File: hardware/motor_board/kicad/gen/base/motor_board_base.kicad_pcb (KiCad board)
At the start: 4 copper layers, 75 x 35 mm, 237 parts, among them J1 BOOMELE_1.27-2x10P, J2 WAFER-SH1.0-6PWB, J3 WAFER-SH1.0-6PWB, J4 S5B-XH-A, Q1 HYG015N04LS1C2, Q2 HYG015N04LS1C2, Q3 HYG015N04LS1C2, Q4 HYG015N04LS1C2, Q5 HYG015N04LS1C2, Q6 HYG015N04LS1C2, Q7 HYG015N04LS1C2, Q8 HYG015N04LS1C2, U1 STM32G474RET6, U10 SN74LVC3G17DCUR, U11 TPS22945DCKR, U12 TPS22945DCKR, U13 LM74502DDFR, U14 74LVC1G17SE-7, U2 DRV8323RHRGZR, U3 DRV8316CRRGFR, U4 DRV8316CRRGFR, U5 AP2112K-3.3TRG1, U6 SN74LVC08APWR, U7 INA239AIDGSR, U8 BQ76907RGRR, U9 SN74LVC3G17DCUR

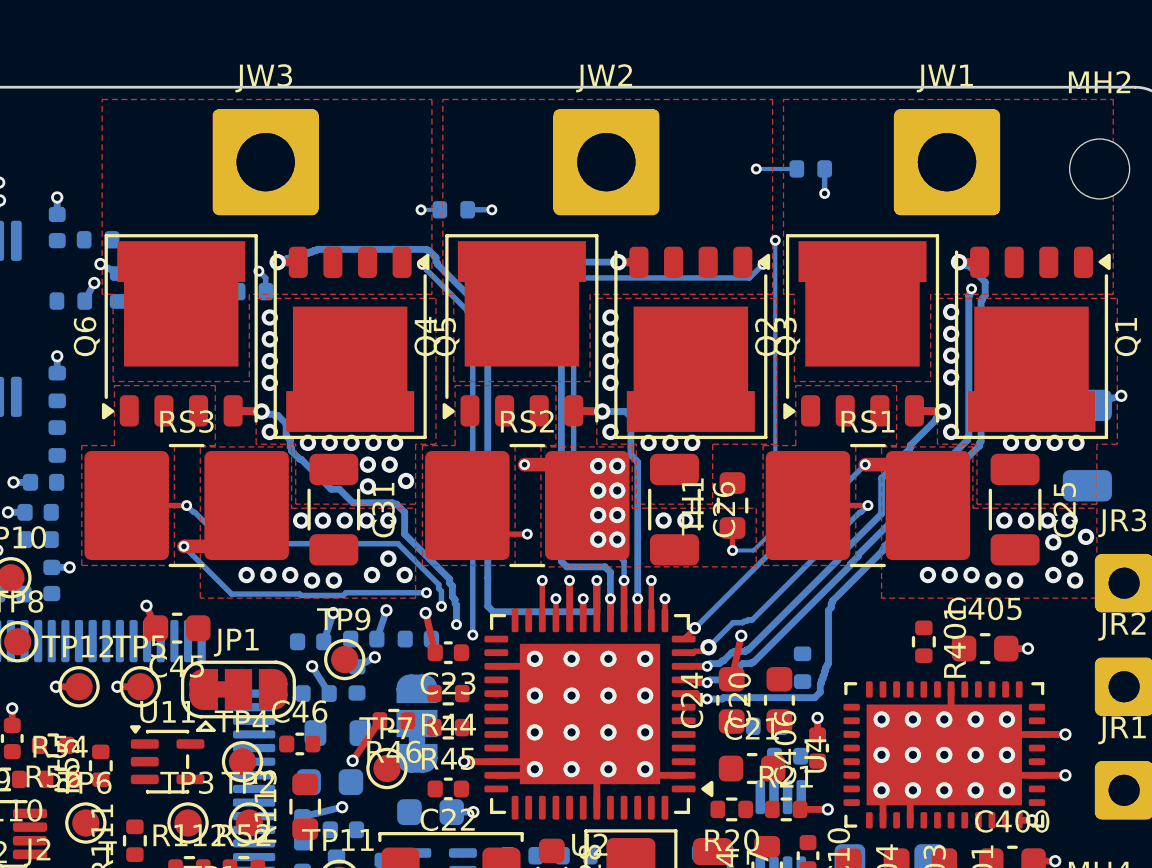
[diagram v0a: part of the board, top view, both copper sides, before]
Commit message: motor_board routing block 1: weapon gate drive + Kelvin sense (all 15 nets, DRC 0)
Scripted interactive-style routing: grid router (router.py) for open ground, hand-planned
fixed geometry (route_blocks.py) for U2's fan-out and the bundle orderings. Base-board
edits (base_edits.py): NT1-3 flat in the shunt pad gaps, R24/R62 moved, five via-field
vias dropped for channels, L3 VBAT feed trimmed to leave a front lane strip for the
divided-phase/NTC lines. Min via 0.4/0.2, Gate class 0.25 mm.

Co-Authored-By: Claude Opus 5.5 (1M context) <noreply@anthropic.com>
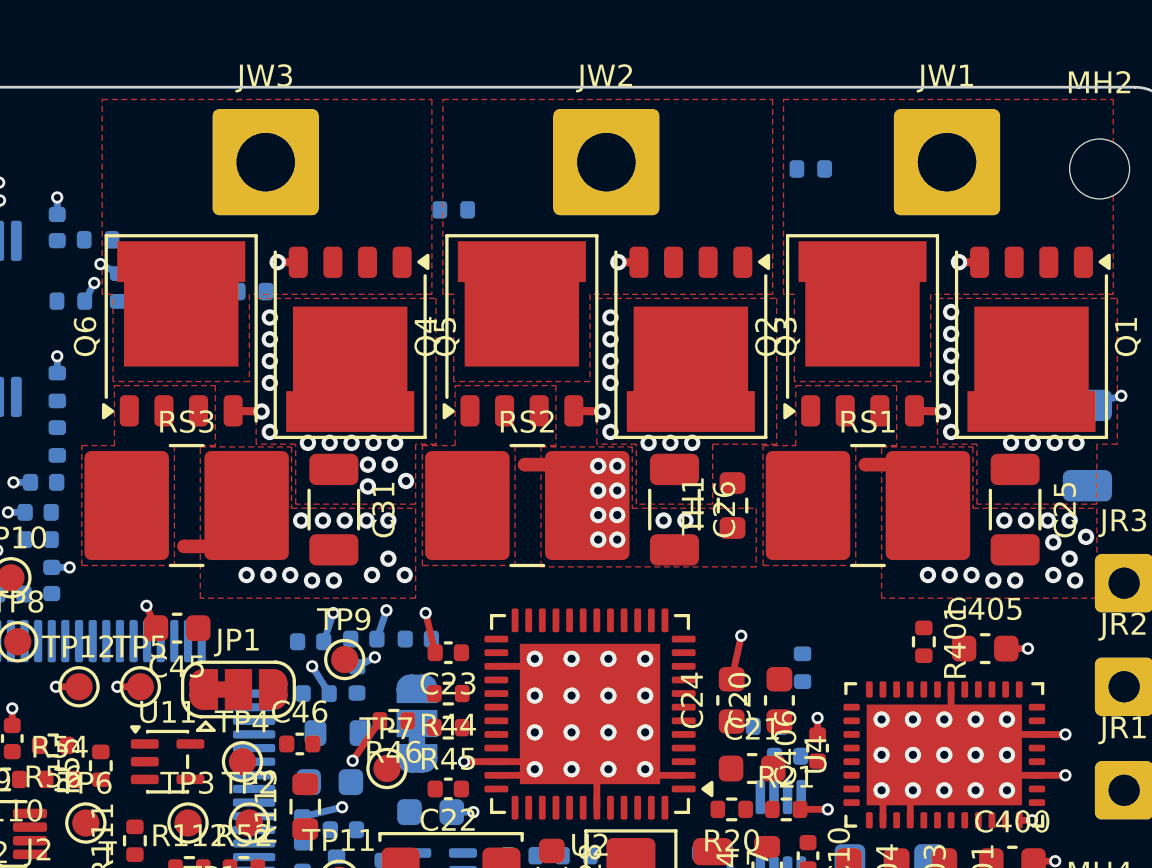
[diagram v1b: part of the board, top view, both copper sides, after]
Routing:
- net /weapon/W_GHC: track 26.9 -> 0.76 mm, vias 2 -> 1
- net /weapon/W_GHA: track 24.5 -> 0.76 mm, vias 2 -> 1
- net /weapon/W_B: track 21.8 -> 0.00 mm, vias 3 -> 0
- net /weapon/W_C: track 21.1 -> 0.00 mm, vias 4 -> 0
- net /weapon/W_A: track 20.6 -> 0.00 mm, vias 3 -> 0
- net /weapon/W_GLC: track 20.1 -> 1.05 mm, vias 3 -> 1
- net /weapon/W_SLC: track 17.3 -> 0.00 mm, vias 3 -> 0
- net /weapon/W_GHB: track 17.2 -> 0.76 mm, vias 2 -> 1
- net /weapon/W_SNC: track 15.3 -> 0.00 mm, vias 3 -> 0
- net /weapon/W_GLA: track 15.1 -> 1.05 mm, vias 2 -> 1
- net W_NTC: track 13.3 -> 0.00 mm, vias 2 -> 0
- net /weapon/W_SLA: track 9.90 -> 0.00 mm, vias 2 -> 0
- net /weapon/W_SNB: track 9.75 -> 0.00 mm, vias 2 -> 0
- net /weapon/W_SNA: track 9.31 -> 0.00 mm, vias 2 -> 0
- net /weapon/W_GLB: track 9.48 -> 1.05 mm, vias 2 -> 1
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
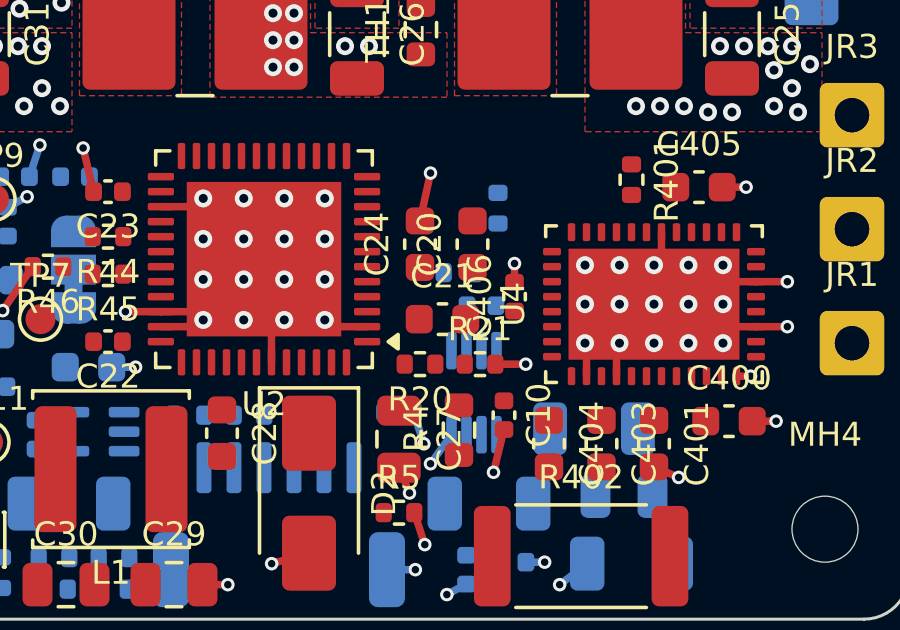
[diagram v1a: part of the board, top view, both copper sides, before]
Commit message: motor_board routing block 2: U2 local (buck loop, charge pump lanes, straps, FB/EN dividers), DRC 0
Charge-pump caps C20/C21 swapped (C20 flipped) so pins 5/4/3 fan out without crossing;
R20/R21 0.1 mm rearward for courtyard room.

Co-Authored-By: Claude Opus 5.5 (1M context) <noreply@anthropic.com>
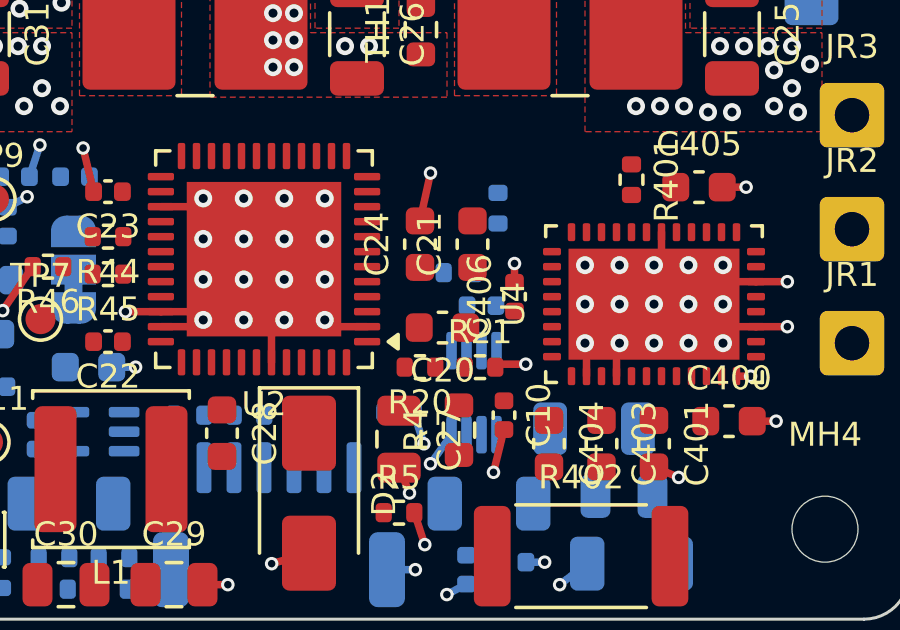
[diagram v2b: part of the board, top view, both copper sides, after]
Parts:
- moved C20 2.95 mm to (159.4, 95.3), turned to 180 degrees
- moved C21 2.69 mm to (160.4, 92.5), turned to 90 degrees
- moved R20 0.10 mm to (158.7, 96.6)
- moved R21 0.10 mm to (160.7, 96.6)
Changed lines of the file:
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@@
 	(footprint "Resistor_SMD:R_0402_1005Metric"
 		(layer "F.Cu")
-		(at 158.7 96.5 180)
+		(at 158.7 96.6 180)
 		(descr "Resistor SMD 0402 (1005 Metric), square (rectangular) end terminal, IPC-7351 nominal, (Body size source: IPC-SM-782 page 72, https://www.pcb-3d.com/wordpress/wp-content/uploads/ipc-sm-782a_amendment_1_and_2.pdf)")
 		(tags "resistor")
@@
 	(footprint "Resistor_SMD:R_0402_1005Metric"
 		(layer "F.Cu")
-		(at 160.7 96.5)
+		(at 160.7 96.6)
 		(descr "Resistor SMD 0402 (1005 Metric), square (rectangular) end terminal, IPC-7351 nominal, (Body size source: IPC-SM-782 page 72, https://www.pcb-3d.com/wordpress/wp-content/uploads/ipc-sm-782a_amendment_1_and_2.pdf)")
 		(tags "resistor")
@@
 	(footprint "Capacitor_SMD:C_0603_1608Metric"
 		(layer "F.Cu")
-		(at 159.45 95)
+		(at 160.45 92.5 90)
 		(descr "Capacitor SMD 0603 (1608 Metric), square (rectangular) end terminal, IPC-7351 nominal, (Body size source: IPC-SM-782 page 76, https://www.pcb-3d.com/wordpress/wp-content/uploads/ipc-sm-782a_amendment_1_and_2.pdf)")
 		(tags "capacitor")
 		(property "Reference" "C21"
-			(at 0 -1.43 0)
+			(at 0 -1.43 90)
 			(layer "F.SilkS")
 			(effects
@@
 		)
 		(property "Value" "1uF 50V"
-			(at 0 1.43 0)
+			(at 0 1.43 90)
 			(layer "F.Fab")
 			(hide yes)
@@
 		)
 		(property "Datasheet" ""
-			(at 0 0 0)
+			(at 0 0 90)
 			(layer "F.Fab")
 			(hide yes)
@@
 		)
 		(property "Description" "Unpolarized capacitor"
-			(at 0 0 0)
+			(at 0 0 90)
 			(layer "F.Fab")
 			(hide yes)
@@
 		)
 		(property "KiLib_Generator" "SMD_2terminal_chip_molded"
-			(at 0 0 0)
+			(at 0 0 90)
 			(layer "F.SilkS")
 			(hide yes)
@@
 		)
 		(property "LCSC" "C15849"
-			(at 0 0 0)
+			(at 0 0 90)
 			(layer "F.SilkS")
 			(hide yes)
@@
 		)
 		(fp_text user "${REFERENCE}"
-			(at 0 0 0)
+			(at 0 0 90)
 			(layer "F.Fab")
 			(effects
@@
 		)
 		(pad "1" smd roundrect
-			(at -0.775 0)
+			(at -0.775 0 90)
 			(size 0.9 0.95)
 			(layers "F.Cu" "F.Mask" "F.Paste")
@@
 		)
 		(pad "2" smd roundrect
-			(at 0.775 0)
+			(at 0.775 0 90)
 			(size 0.9 0.95)
 			(layers "F.Cu" "F.Mask" "F.Paste")
@@
 	(footprint "Capacitor_SMD:C_0603_1608Metric"
 		(layer "F.Cu")
-		(at 160.45 92.5 90)
+		(at 159.45 95.28 180)
 		(descr "Capacitor SMD 0603 (1608 Metric), square (rectangular) end terminal, IPC-7351 nominal, (Body size source: IPC-SM-782 page 76, https://www.pcb-3d.com/wordpress/wp-content/uploads/ipc-sm-782a_amendment_1_and_2.pdf)")
 		(tags "capacitor")
 		(property "Reference" "C20"
-			(at 0 -1.43 90)
+			(at 0 -1.43 180)
 			(layer "F.SilkS")
 			(effects
@@
 		)
 		(property "Value" "47nF 50V"
-			(at 0 1.43 90)
+			(at 0 1.43 180)
 			(layer "F.Fab")
 			(hide yes)
@@
 		)
 		(property "Datasheet" ""
-			(at 0 0 90)
+			(at 0 0 180)
 			(layer "F.Fab")
 			(hide yes)
@@
 		)
 		(property "Description" "Unpolarized capacitor"
-			(at 0 0 90)
+			(at 0 0 180)
 			(layer "F.Fab")
 			(hide yes)
@@
 		)
 		(property "KiLib_Generator" "SMD_2terminal_chip_molded"
-			(at 0 0 90)
+			(at 0 0 180)
 			(layer "F.SilkS")
 			(hide yes)
@@
 		)
 		(property "LCSC" "C1622"
-			(at 0 0 90)
+			(at 0 0 180)
 			(layer "F.SilkS")
 			(hide yes)
@@
 		(duplicate_pad_numbers_are_jumpers no)
 		(fp_line
-			(start -0.14058 -0.51)
-			(end 0.14058 -0.51)
+			(start -0.14058 0.51)
+			(end 0.14058 0.51)
 			(stroke
 				(width 0.12)
@@
 		)
 		(fp_line
-			(start -0.14058 0.51)
-			(end 0.14058 0.51)
+			(start -0.14058 -0.51)
+			(end 0.14058 -0.51)
 			(stroke
 				(width 0.12)
@@
 		)
 		(fp_text user "${REFERENCE}"
-			(at 0 0 90)
+			(at 0 0 180)
 			(layer "F.Fab")
 			(effects
@@
 		)
 		(pad "1" smd roundrect
-			(at -0.775 0 90)
+			(at -0.775 0 180)
 			(size 0.9 0.95)
 			(layers "F.Cu" "F.Mask" "F.Paste")
@@
 		)
 		(pad "2" smd roundrect
-			(at 0.775 0 90)
+			(at 0.775 0 180)
 			(size 0.9 0.95)
 			(layers "F.Cu" "F.Mask" "F.Paste")

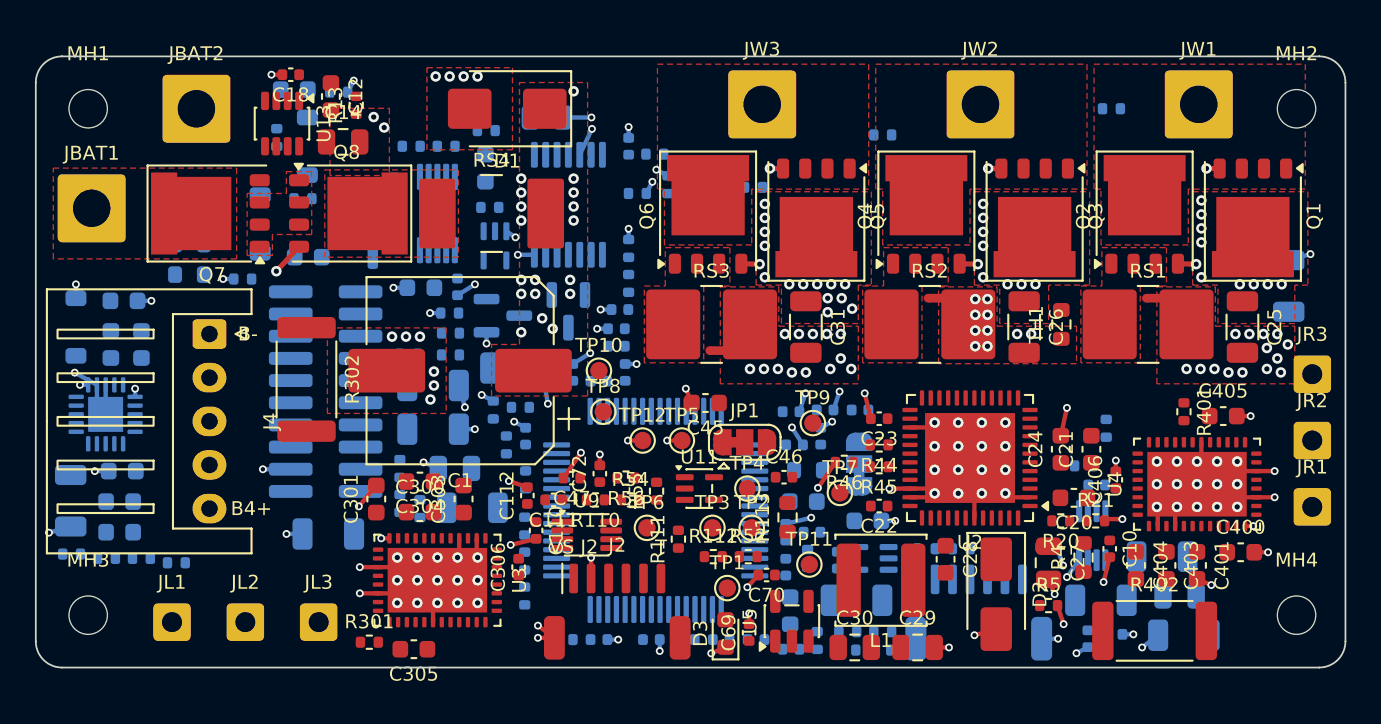
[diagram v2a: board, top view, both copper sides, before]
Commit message: motor_board routing: ROUTING_PLAN.md; U1 fan-out under its body (39 pins); test pads moved off U1's footprint; GND drop-via block; geo.py clearance helper
Co-Authored-By: Claude Opus 5.5 (1M context) <noreply@anthropic.com>
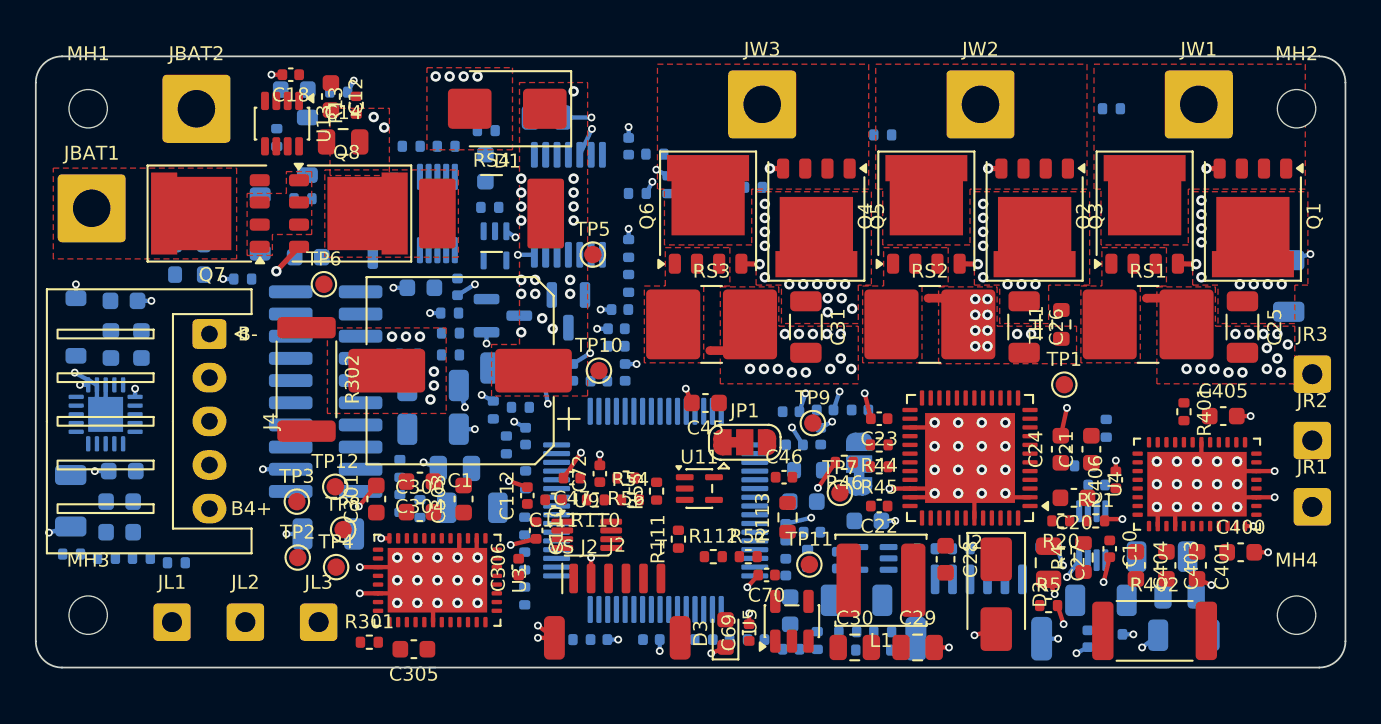
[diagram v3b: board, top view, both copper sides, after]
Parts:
- moved TP2 26.1 mm to (115.0, 98.7)
- moved TP4 24.0 mm to (117.2, 99.2)
- moved TP3 23.8 mm to (115.0, 95.5)
- moved TP6 23.2 mm to (116.5, 83.0)
- moved TP1 22.5 mm to (158.9, 88.8)
- moved TP12 17.8 mm to (117.2, 94.7)
- moved TP8 16.4 mm to (117.6, 97.1)
- moved TP5 11.8 mm to (131.9, 81.3)
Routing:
- net GND: track 96.5 -> 94.8 mm, vias 178 -> 176
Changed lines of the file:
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@@
 	(footprint "TestPoint:TestPoint_Pad_D1.0mm"
 		(layer "F.Cu")
-		(at 134.75 92)
+		(at 117.15 94.65)
 		(descr "SMD pad as test Point, diameter 1.0mm")
 		(tags "test point SMD pad")
@@
 	(footprint "TestPoint:TestPoint_Pad_D1.0mm"
 		(layer "F.Cu")
-		(at 138.75 97)
+		(at 114.95 95.5)
 		(descr "SMD pad as test Point, diameter 1.0mm")
 		(tags "test point SMD pad")
@@
 	(footprint "TestPoint:TestPoint_Pad_D1.0mm"
 		(layer "F.Cu")
-		(at 139.6 100.45)
+		(at 158.9 88.8)
 		(descr "SMD pad as test Point, diameter 1.0mm")
 		(tags "test point SMD pad")
@@
 	(footprint "TestPoint:TestPoint_Pad_D1.0mm"
 		(layer "F.Cu")
-		(at 137 92)
+		(at 131.9 81.35)
 		(descr "SMD pad as test Point, diameter 1.0mm")
 		(tags "test point SMD pad")
@@
 	(footprint "TestPoint:TestPoint_Pad_D1.0mm"
 		(layer "F.Cu")
-		(at 140.75 94.75)
+		(at 117.2 99.25)
 		(descr "SMD pad as test Point, diameter 1.0mm")
 		(tags "test point SMD pad")
@@
 	(footprint "TestPoint:TestPoint_Pad_D1.0mm"
 		(layer "F.Cu")
-		(at 141 97)
+		(at 115 98.7)
 		(descr "SMD pad as test Point, diameter 1.0mm")
 		(tags "test point SMD pad")
@@
 	(footprint "TestPoint:TestPoint_Pad_D1.0mm"
 		(layer "F.Cu")
-		(at 132.5 90.35)
+		(at 117.6 97.1)
 		(descr "SMD pad as test Point, diameter 1.0mm")
 		(tags "test point SMD pad")
@@
 	(footprint "TestPoint:TestPoint_Pad_D1.0mm"
 		(layer "F.Cu")
-		(at 135 97)
+		(at 116.5 83.05)
 		(descr "SMD pad as test Point, diameter 1.0mm")
 		(tags "test point SMD pad")
@@
 	)
 	(segment
-		(start 137 92)
-		(end 136.155 92)
-		(width 0.25)
-		(layer "F.Cu")
-		(net "GND")
-	)
-	(segment
 		(start 169.9 95.25)
 		(end 169.149999 95.25)
@@
 	)
 	(segment
-		(start 134.75 92)
-		(end 133.905 92)
-		(width 0.25)
-		(layer "F.Cu")
-		(net "GND")
-	)
-	(segment
 		(start 155 102.8)
 		(end 153.755 103.15)
@@
 	)
 	(via
-		(at 133.905 92)
-		(size 0.45)
-		(drill 0.25)
-		(layers "F.Cu" "B.Cu")
-		(net "GND")
-	)
-	(via
 		(at 154.174999 90.975)
 		(size 0.6)
@@
 		(layers "F.Cu" "B.Cu")
 		(net "GND")
-	)
-	(via
-		(at 136.155 92)
-		(size 0.45)
-		(drill 0.25)
-		(layers "F.Cu" "B.Cu")
-		(net "GND")

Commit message: motor_board routing blocks 6a/6: U3/U4 charge pump + VM caps re-placed to pin order (U4 mirrors U3, C400 on the bottom), AVDD/FBBK/SWBK hookups; TP8/TP12 moved again
Co-Authored-By: Claude Opus 5.5 (1M context) <noreply@anthropic.com>
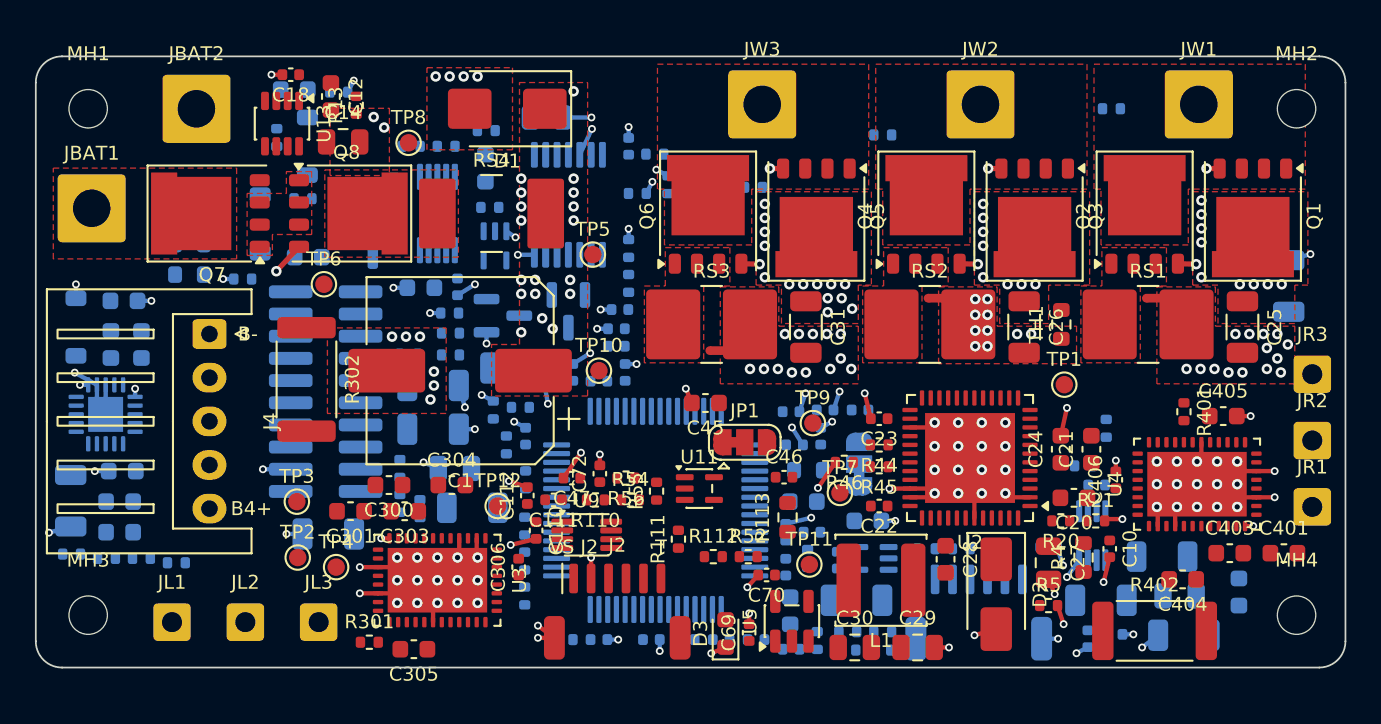
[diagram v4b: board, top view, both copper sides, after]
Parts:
- C400: moved to B.Cu
- moved TP8 22.5 mm to (121.3, 75.0)
- moved TP12 9.36 mm to (126.5, 95.8)
- moved C401 5.02 mm to (171.5, 98.5), turned to 0 degrees
- moved C403 3.69 mm to (168.4, 98.5), turned to 0 degrees
- moved C303 3.45 mm to (121.1, 96.0), turned to 180 degrees
- moved C404 2.79 mm to (165.7, 100.0), turned to 180 degrees
- moved C300 2.36 mm to (120.2, 94.5), turned to 180 degrees
- moved C400 2.28 mm to (168.9, 100.7), turned to -90 degrees
- moved C304 1.84 mm to (123.8, 94.5), turned to 0 degrees
- moved C301 1.63 mm to (118.0, 96.0), turned to 180 degrees
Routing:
- net GND: track 94.8 -> 91.5 mm, vias 176 -> 173
